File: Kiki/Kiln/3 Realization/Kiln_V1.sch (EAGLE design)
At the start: 22 parts, among them T1 2N3904, T2 2N3904, T3 2N3904, T4 2N3904, X1 3.5mm term

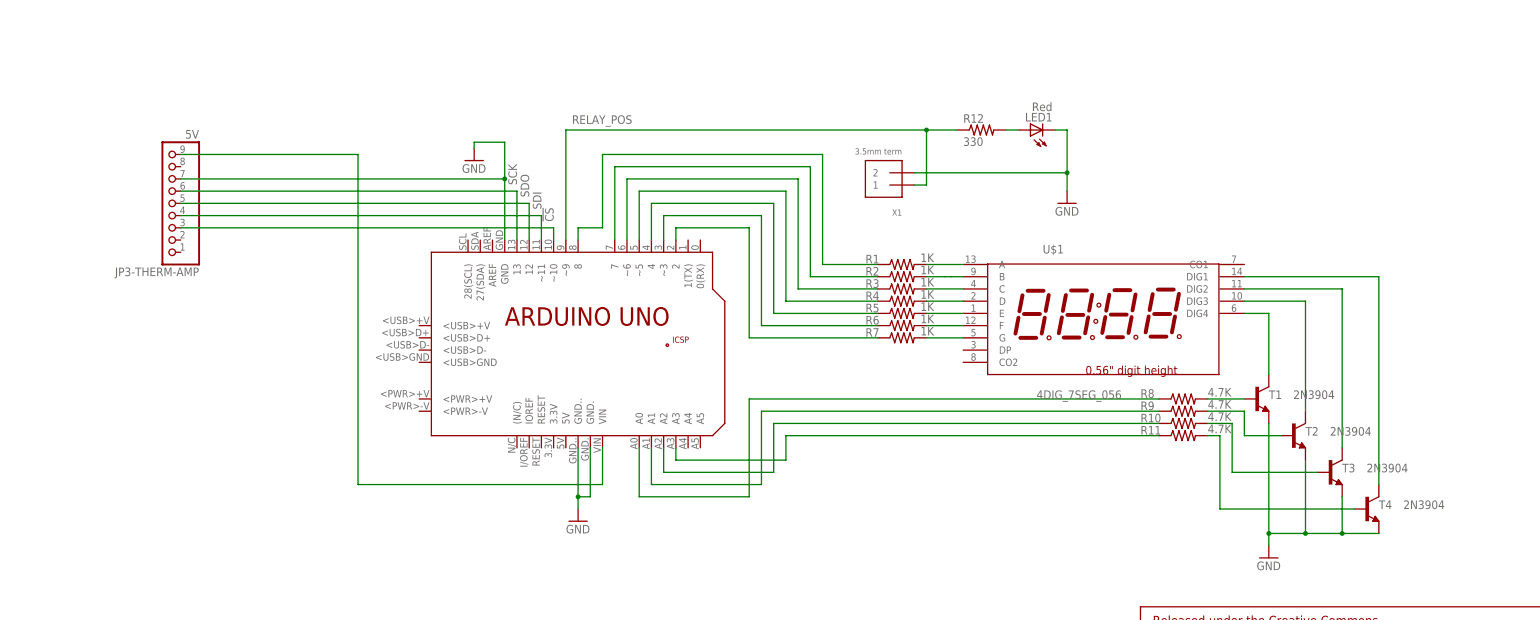
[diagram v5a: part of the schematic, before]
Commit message: Update: nets are named I had used Wire instead of Net, so I had to rework everything. But it's done.  All nets are named.
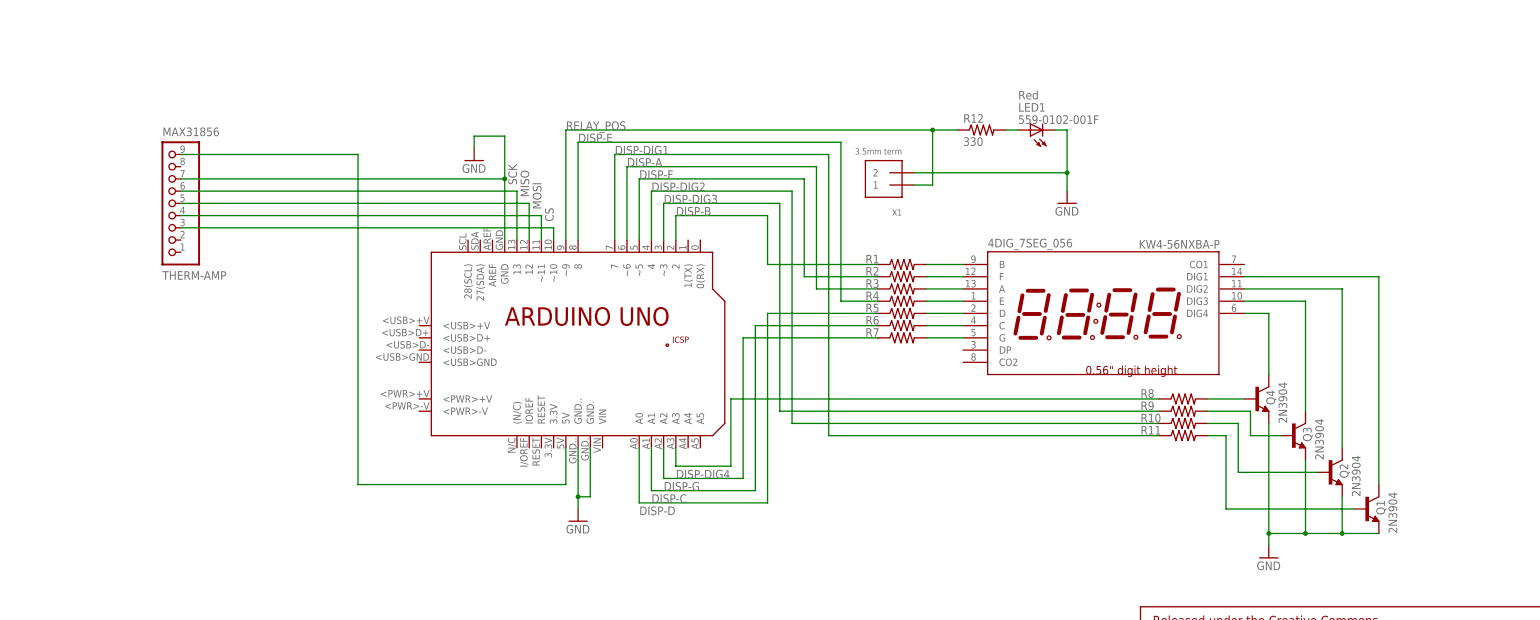
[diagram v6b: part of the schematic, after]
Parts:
- 4DIG_7SEG_056: value 4DIG_7SEG_056 -> KW4-56NXBA-P
- LED1: value Red -> 559-0102-001F; LABEL (none) -> Red
- R1, R2, R3, R4, R5, R6, R7: device SparkFun-Resistors:1KOHM-1/10W-1%(0603) -> 1-Generic:RESISTOR1206
- R10, R11, R8, R9: device SparkFun-Resistors:4.7KOHM-1/10W-1%(0603) -> 1-Generic:RESISTOR1206
- R12: device SparkFun-Resistors:330OHM1/10W1%(0603) -> 1-Generic:RESISTOR1206
- THERM-AMP: value 5V -> MAX31856
- renumbered JP3-THERM-AMP to THERM-AMP, T1 to Q4, T2 to Q3, T3 to Q2, T4 to Q1, U$1 to 4DIG_7SEG_056
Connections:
- net !CS renamed CS
- net N$1 renamed R8
- net N$16 renamed G
- net N$2 renamed R9
- net N$21 renamed R12
- net N$27 renamed DISP-A
- net N$3 renamed R10
- net N$4 renamed R11
- net N$5 renamed DIG4
- net N$6 renamed DIG3
- net N$7 renamed DIG2
- net N$8 renamed DIG1
- net SDI renamed MOSI
- net SDO renamed MISO
- removed net N$10: 4DIG_7SEG_056.A, R1.2
- removed net N$11: 4DIG_7SEG_056.B, R2.2
- removed net N$12: 4DIG_7SEG_056.C, R3.2
- removed net N$13: 4DIG_7SEG_056.D, R4.2
- removed net N$14: 4DIG_7SEG_056.E, R5.2
- removed net N$15: 4DIG_7SEG_056.F, R6.2
- removed net N$17: PCB1.A3, R11.1
- removed net N$18: PCB1.A2, R10.1
- removed net N$19: PCB1.A1, R9.1
- removed net N$20: PCB1.A0, R8.1
- removed net N$22: PCB1.7, R2.1
- removed net N$23: PCB1.2, R7.1
- removed net N$24: PCB1.~3, R6.1
- removed net N$25: PCB1.4, R5.1
- removed net N$26: PCB1.~5, R4.1
- removed net N$31: PCB1.VIN, THERM-AMP.9
- removed net N$9: PCB1.8, R1.1
- new net A: 4DIG_7SEG_056.A, R3.2
- new net B: 4DIG_7SEG_056.B, R1.2
- new net C: 4DIG_7SEG_056.C, R6.2
- new net D: 4DIG_7SEG_056.D, R5.2
- new net DISP-B: PCB1.2, R1.1
- new net DISP-C: PCB1.A1, R6.1
- new net DISP-D: PCB1.A0, R5.1
- new net DISP-DIG1: PCB1.7, R11.1
- new net DISP-DIG2: PCB1.4, R10.1
- new net DISP-DIG3: PCB1.~3, R9.1
- new net DISP-DIG4: PCB1.A3, R8.1
- new net DISP-E: PCB1.8, R4.1
- new net DISP-F: PCB1.~5, R2.1
- new net DISP-G: PCB1.A2, R7.1
- new net E: 4DIG_7SEG_056.E, R4.2
- new net F: 4DIG_7SEG_056.F, R2.2
- new net VIN: PCB1.5V, THERM-AMP.9

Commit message: Added: start button Added pads for soldering the Start Button. Also added the 7seg4dig library, which seems wasn't added. Note: Copy to Library was grayed out.
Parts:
- added START-BTN, START-GND: WIREPAD2,54/1,1, wirepad:WIREPAD2,54/1,1
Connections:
- new net START-NET: PCB1.A4, START-BTN.P
- net GND: now also START-GND.P
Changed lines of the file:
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@@
 <part name="R12" library="1-Generic" deviceset="RESISTOR" device="1206" value="330"/>
 <part name="4DIG_7SEG_056" library="7-seg-disp" deviceset="4DIG_7SEG_056" device="" value="KW4-56NXBA-P"/>
+<part name="GND5" library="supply1" deviceset="GND" device=""/>
+<part name="START-BTN" library="wirepad" deviceset="WIREPAD" device="2,54/1,1"/>
+<part name="START-GND" library="wirepad" deviceset="WIREPAD" device="2,54/1,1"/>
 </parts>
 <sheets>
@@
 <attribute name="NAME" x="146.05" y="36.576" size="1.778" layer="95"/>
 <attribute name="VALUE" x="194.31" y="38.1" size="1.778" layer="96" rot="R180"/>
+</instance>
+<instance part="GND5" gate="1" x="105.41" y="-15.24"/>
+<instance part="START-BTN" gate="G$1" x="107.95" y="-6.35" smashed="yes" rot="R180">
+<attribute name="NAME" x="109.093" y="-5.6642" size="1.778" layer="95"/>
+<attribute name="VALUE" x="109.093" y="-8.128" size="1.778" layer="96"/>
+</instance>
+<instance part="START-GND" gate="G$1" x="107.95" y="-10.16" smashed="yes" rot="R180">
+<attribute name="NAME" x="109.093" y="-12.0142" size="1.778" layer="95"/>
+<attribute name="VALUE" x="109.093" y="-14.478" size="1.778" layer="96"/>
 </instance>
 </instances>
@@
 <junction x="60.96" y="-15.24"/>
 </segment>
+<segment>
+<pinref part="START-GND" gate="G$1" pin="P"/>
+<pinref part="GND5" gate="1" pin="GND"/>
+<wire x1="105.41" y1="-10.16" x2="105.41" y2="-12.7" width="0.1524" layer="91"/>
+</segment>
 </net>
 <net name="RELAY_POS" class="0">
@@
 </segment>
 </net>
+<net name="START-NET" class="0">
+<segment>
+<pinref part="START-BTN" gate="G$1" pin="P"/>
+<wire x1="105.41" y1="-6.35" x2="83.82" y2="-6.35" width="0.1524" layer="91"/>
+<pinref part="PCB1" gate="G$1" pin="A4"/>
+<wire x1="83.82" y1="-5.08" x2="83.82" y2="-6.35" width="0.1524" layer="91"/>
+</segment>
+</net>

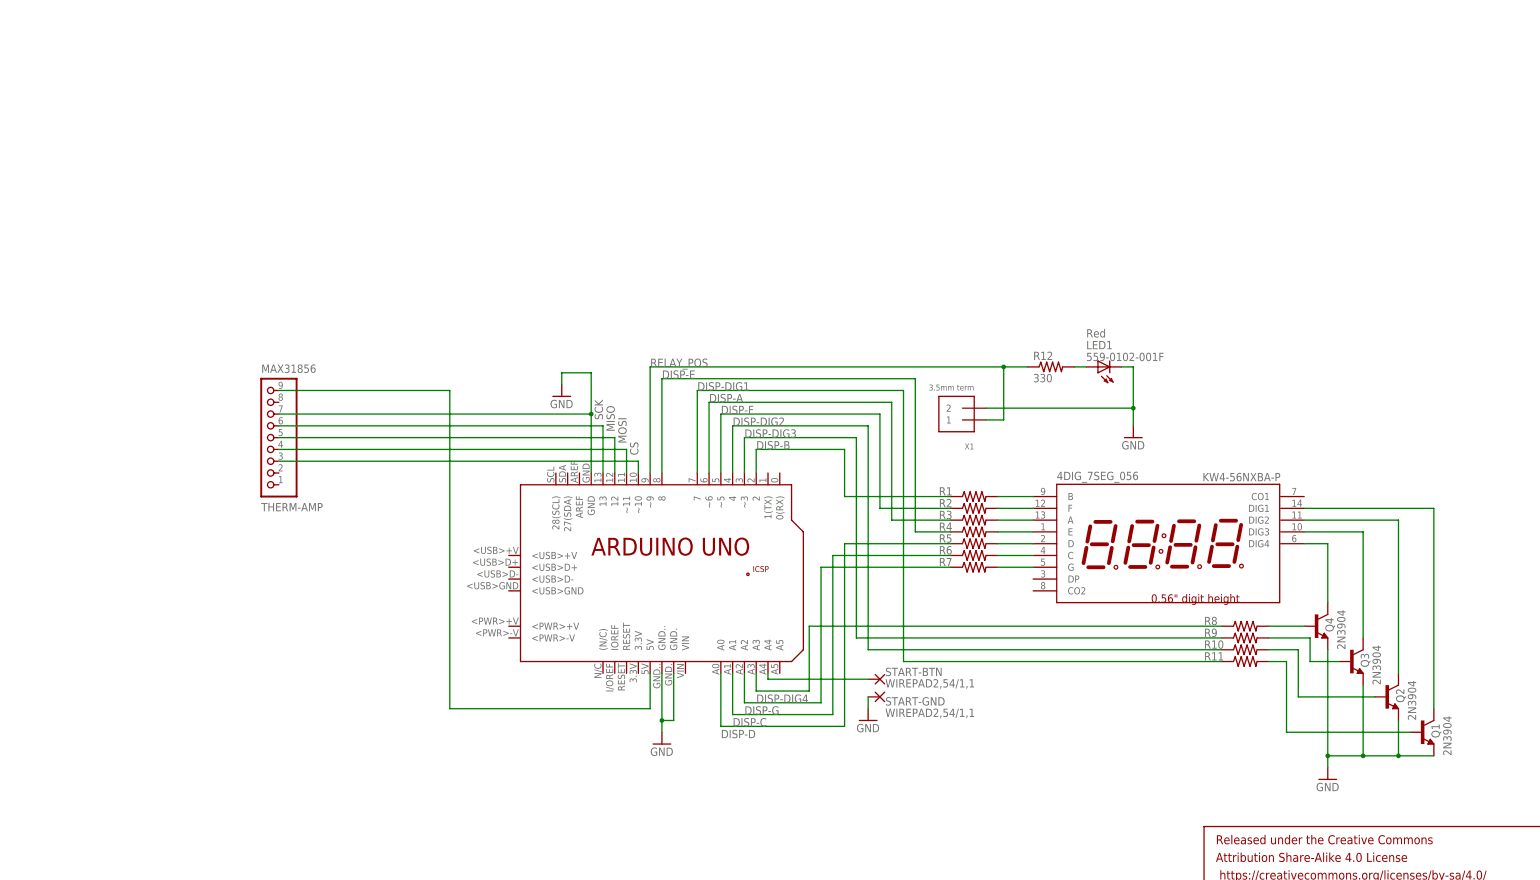
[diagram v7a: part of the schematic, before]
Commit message: Update: final comments Fixed all the things listed in the final comments
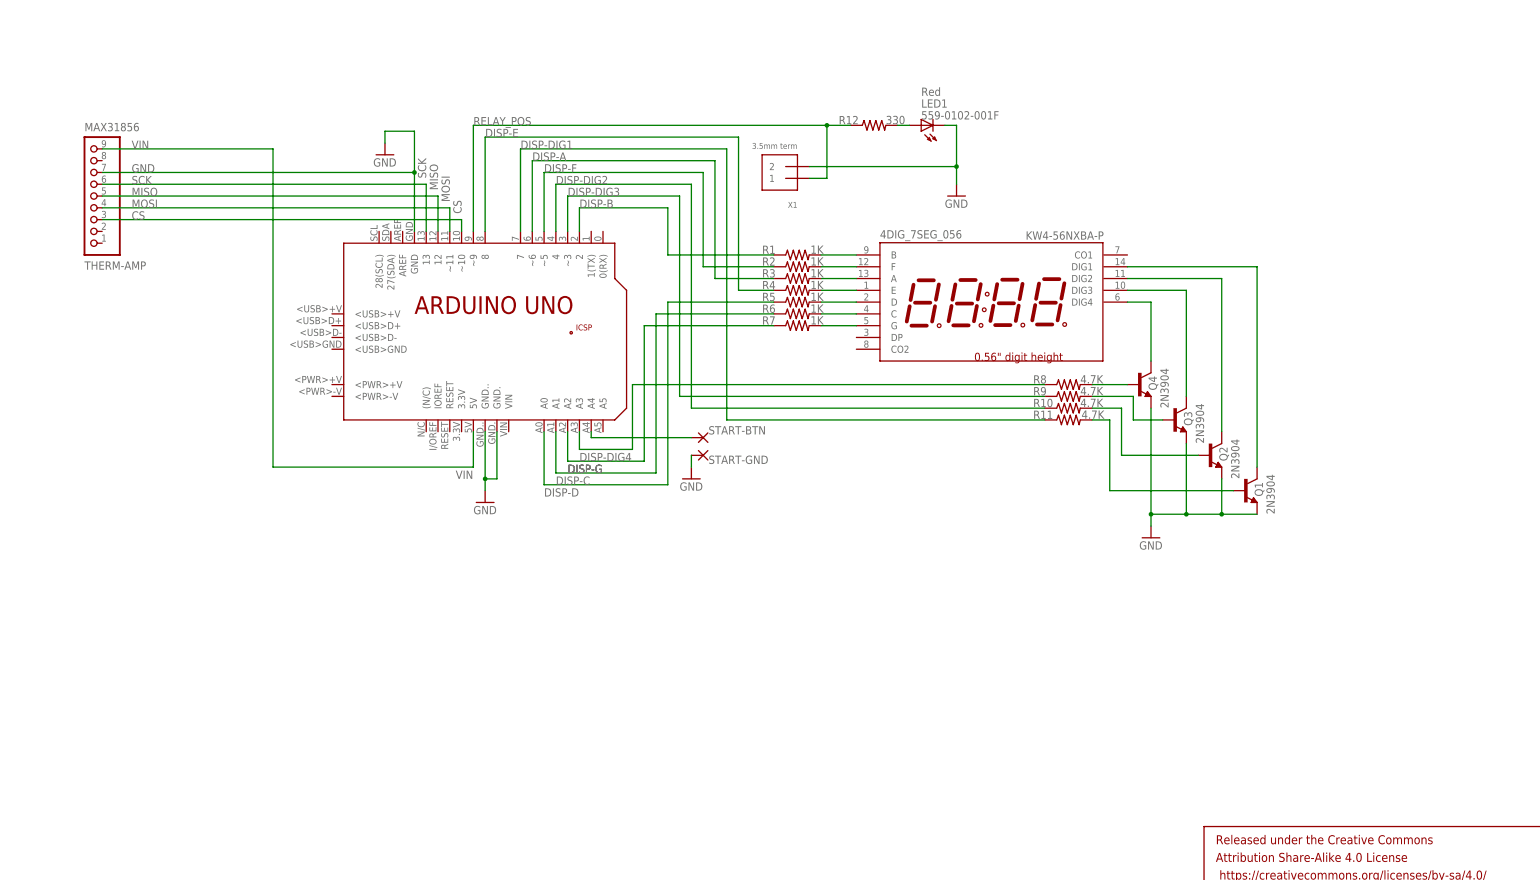
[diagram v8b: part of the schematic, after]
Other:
- moved on the sheet: 4DIG_7SEG_056, LED1, Q1, Q2, Q3, Q4, R1, R10, R11, R12, R2, R3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
